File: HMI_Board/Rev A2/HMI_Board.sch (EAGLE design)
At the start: 34 parts, among them SW1 B3FS-1015, SW2 B3FS-1015, SW3 B3FS-1015, SW4 B3FS-1015, SW5 B3FS-1015, SW6 B3FS-1015, U1 90814-0208, U2 90814-0206

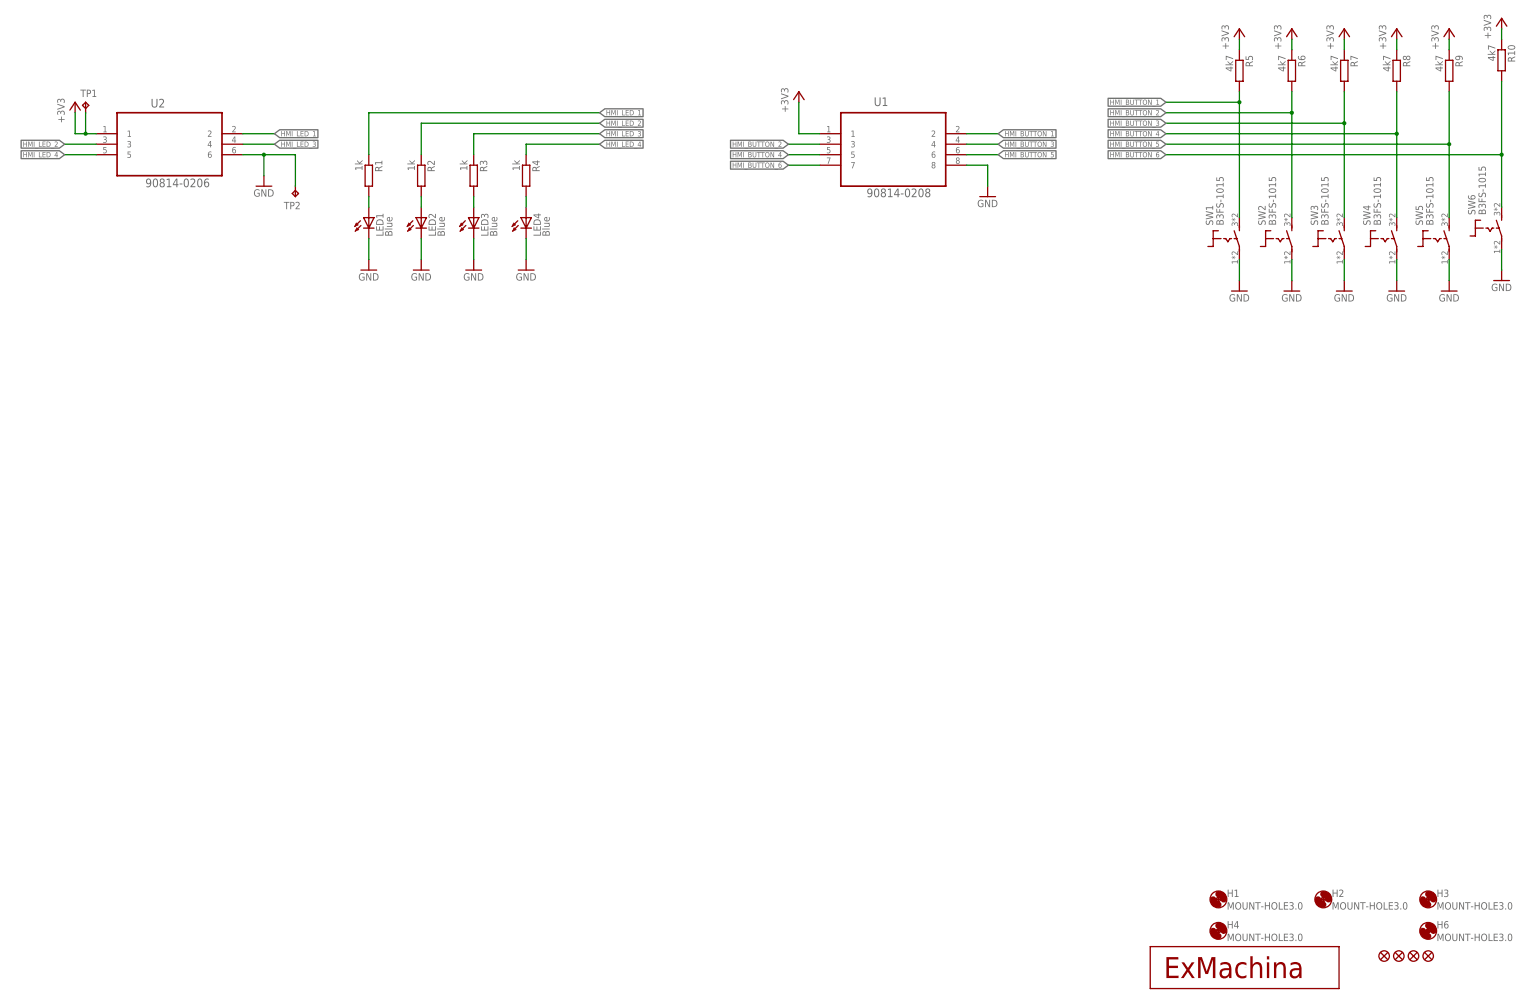
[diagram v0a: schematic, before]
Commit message: Add MDP folder to HMI Board rev A2
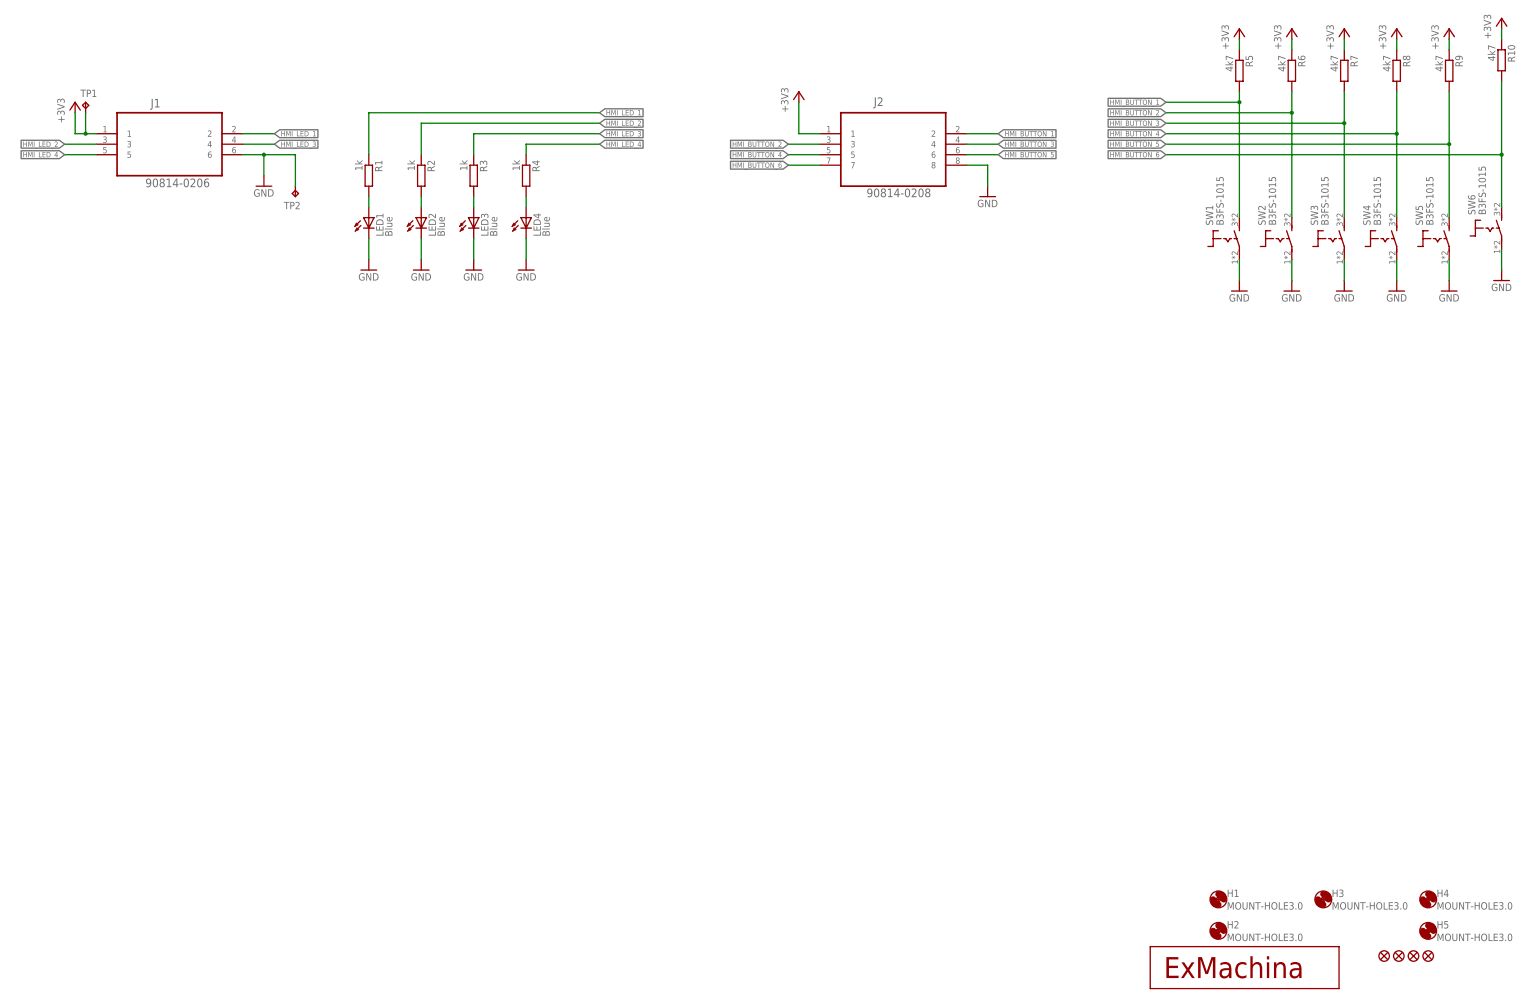
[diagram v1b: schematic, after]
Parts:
- renumbered H6 to H5, U$1 to T1, U1 to J2, U2 to J1
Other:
- moved on the sheet: H2, H3, H4
